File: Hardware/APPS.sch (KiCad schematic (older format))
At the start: 20 parts, among them SW1 SW_Push, U1 STM32F103C8Tx, Y1 Crystal 8 MHz

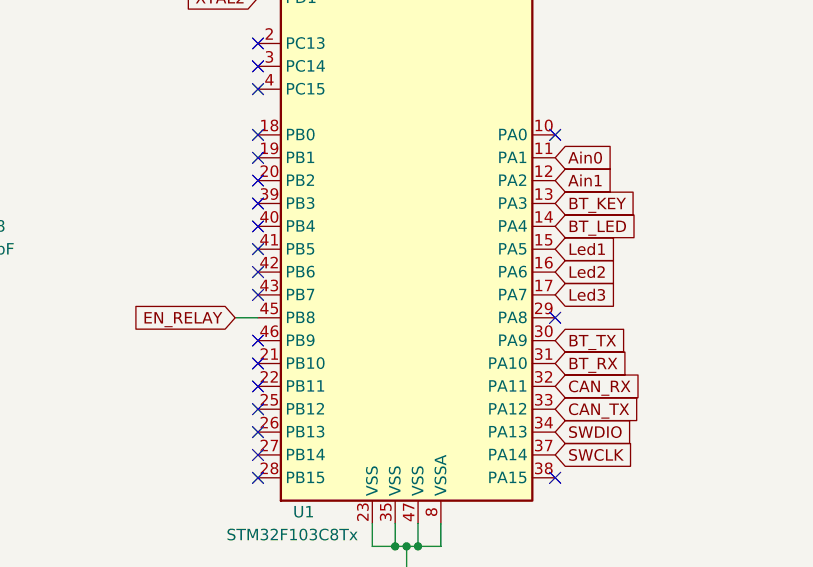
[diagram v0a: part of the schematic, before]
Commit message: Positioned Bluetooth module
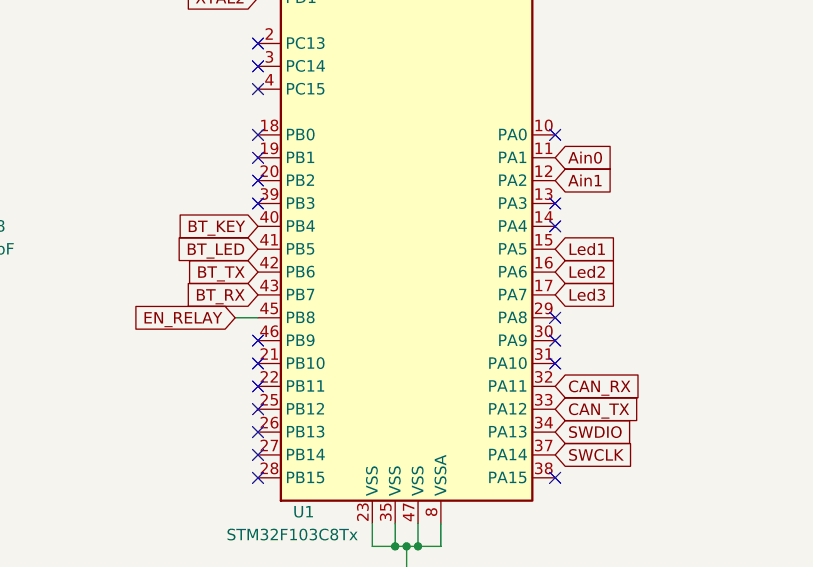
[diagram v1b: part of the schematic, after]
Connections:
- net BT_KEY: now also U1.40 (PB4); no longer U1.13 (PA3)
- net BT_LED: now also U1.41 (PB5); no longer U1.14 (PA4)
- net BT_RX: now also U1.43 (PB7); no longer U1.31 (PA10)
- net BT_TX: now also U1.42 (PB6); no longer U1.30 (PA9)
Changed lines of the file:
@@
 EESchema Schematic File Version 4
-LIBS:APPS-cache
-EELAYER 29 0
+EELAYER 30 0
 EELAYER END
 $Descr A4 11693 8268
@@
 Text GLabel 5500 5050 2    50   Input ~ 0
 SWCLK
-Text GLabel 5500 4750 2    50   Input ~ 0
-CAN_RX
 Wire Wire Line
 	3250 2550 3250 2300
@@
 NoConn ~ 4200 4650
 NoConn ~ 4200 4550
-NoConn ~ 4200 4350
-NoConn ~ 4200 4250
-NoConn ~ 4200 4150
-NoConn ~ 4200 4050
+NoConn ~ 5500 4050
+NoConn ~ 5500 3950
 NoConn ~ 4200 3950
 NoConn ~ 4200 3850
@@
 Text Notes 7850 2700 0    50   ~ 0
 Debugging Diodes
-Text GLabel 5500 4650 2    50   Input ~ 0
+Text GLabel 4200 4350 0    50   Input ~ 0
 BT_RX
-Text GLabel 5500 4550 2    50   Input ~ 0
+Text GLabel 4200 4250 0    50   Input ~ 0
 BT_TX
 Text GLabel 5500 4150 2    50   Input ~ 0
 Led1
-Text GLabel 5500 3950 2    50   Input ~ 0
+Text GLabel 4200 4050 0    50   Input ~ 0
 BT_KEY
-Text GLabel 5500 4050 2    50   Input ~ 0
+Text GLabel 4200 4150 0    50   Input ~ 0
 BT_LED
+NoConn ~ 5500 4550
+NoConn ~ 5500 4650
+Text GLabel 5500 4750 2    50   Input ~ 0
+CAN_RX
 $EndSCHEMATC

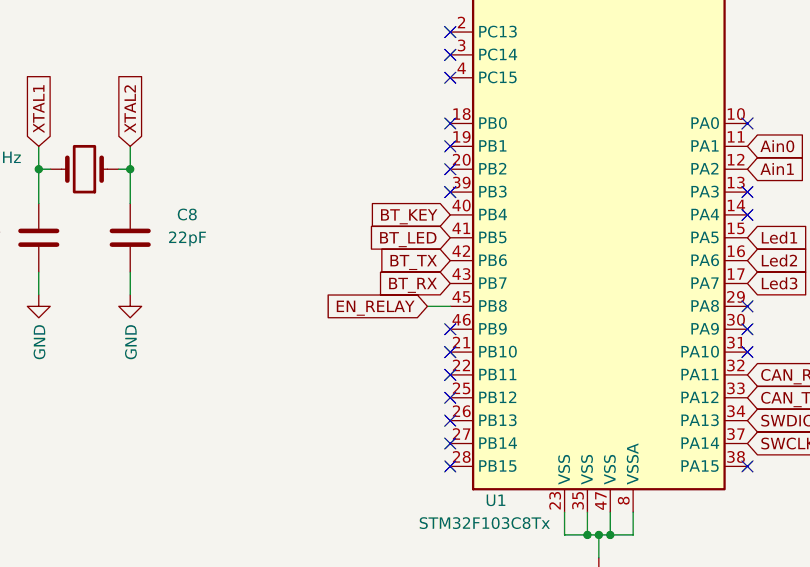
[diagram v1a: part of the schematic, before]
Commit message: Changed HC-05 pins for other Forbot HC-05
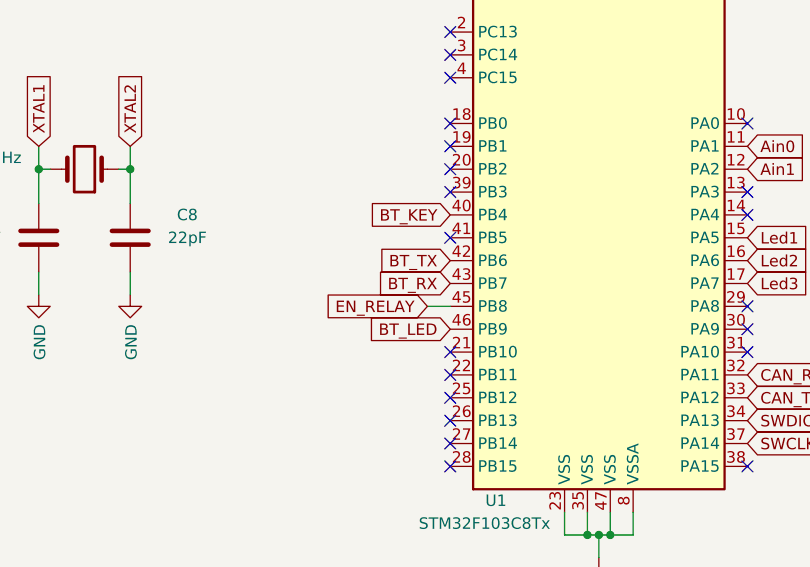
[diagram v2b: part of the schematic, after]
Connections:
- net BT_LED: now also U1.46 (PB9); no longer U1.41 (PB5)
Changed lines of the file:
@@
 NoConn ~ 4200 4750
 NoConn ~ 4200 4650
-NoConn ~ 4200 4550
+NoConn ~ 4200 4150
 NoConn ~ 5500 4050
 NoConn ~ 5500 3950
@@
 Text GLabel 4200 4050 0    50   Input ~ 0
 BT_KEY
-Text GLabel 4200 4150 0    50   Input ~ 0
+Text GLabel 4200 4550 0    50   Input ~ 0
 BT_LED
 NoConn ~ 5500 4550

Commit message: Quick fixes
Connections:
- net BT_KEY: now also U1.46 (PB9); no longer U1.40 (PB4)
- net BT_LED: now also U1.40 (PB4); no longer U1.46 (PB9)
- net BT_RX: now also U1.42 (PB6); no longer U1.43 (PB7)
- net BT_TX: now also U1.43 (PB7); no longer U1.42 (PB6)
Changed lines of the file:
@@
 NoConn ~ 4200 4850
 NoConn ~ 4200 4750
-NoConn ~ 4200 4650
-NoConn ~ 4200 4150
 NoConn ~ 5500 4050
 NoConn ~ 5500 3950
@@
 Text Notes 7850 2700 0    50   ~ 0
 Debugging Diodes
-Text GLabel 4200 4350 0    50   Input ~ 0
-BT_RX
-Text GLabel 4200 4250 0    50   Input ~ 0
-BT_TX
 Text GLabel 5500 4150 2    50   Input ~ 0
 Led1
-Text GLabel 4200 4050 0    50   Input ~ 0
-BT_KEY
-Text GLabel 4200 4550 0    50   Input ~ 0
-BT_LED
 NoConn ~ 5500 4550
 NoConn ~ 5500 4650
 Text GLabel 5500 4750 2    50   Input ~ 0
 CAN_RX
+Text GLabel 4200 4550 0    50   Input ~ 0
+BT_KEY
+NoConn ~ 4200 4650
+Text GLabel 4200 4250 0    50   Input ~ 0
+BT_RX
+Text GLabel 4200 4350 0    50   Input ~ 0
+BT_TX
+NoConn ~ 4200 4150
+Text GLabel 4200 4050 0    50   Input ~ 0
+BT_LED
 $EndSCHEMATC

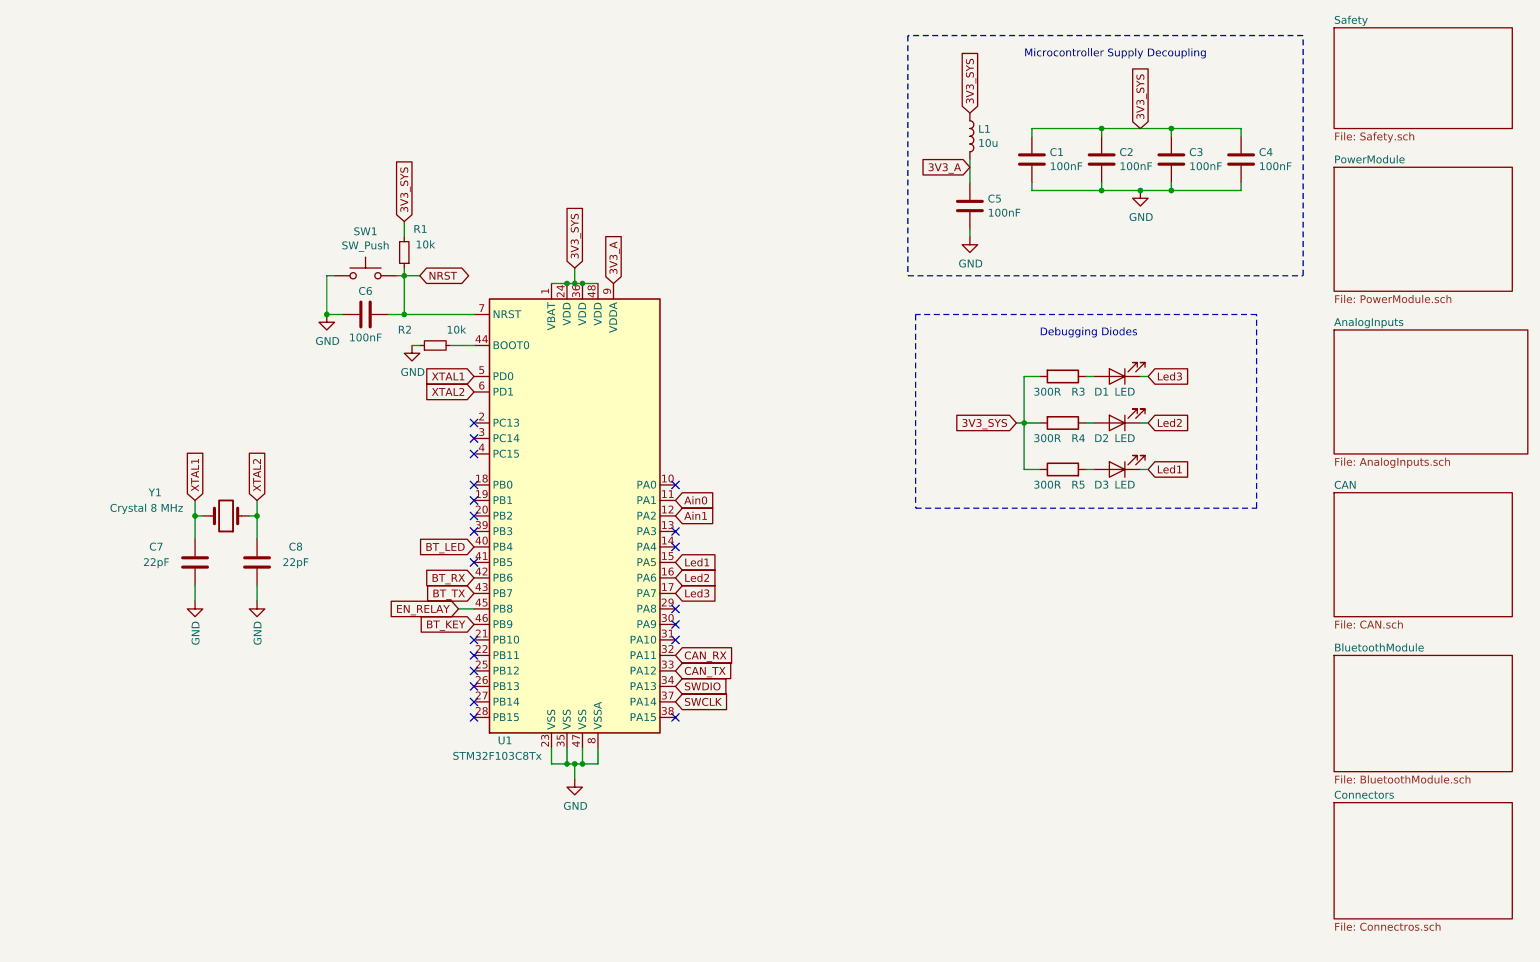
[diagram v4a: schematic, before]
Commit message: Components labels placed
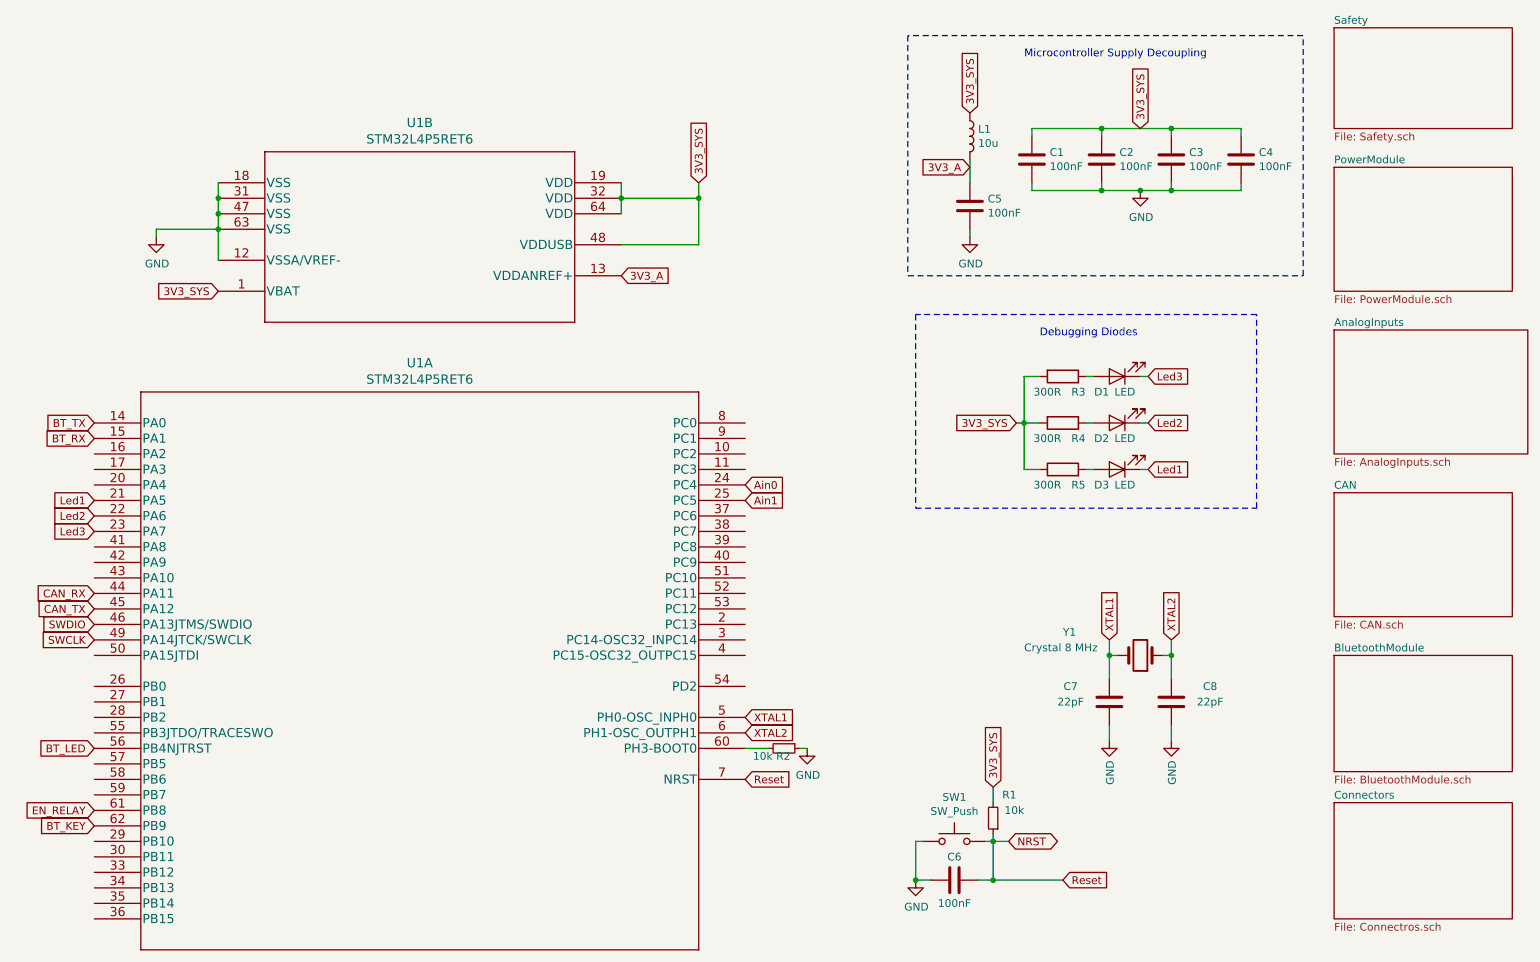
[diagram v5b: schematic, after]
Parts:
- removed U1: STM32F103C8Tx, Package_QFP:LQFP-48_7x7mm_P0.5mm, symbol MCU_ST_STM32F1:STM32F103C8Tx
- added U1: STM32L4P5RET6, footprints:STM32L4P5RET6, symbol 2021-05-10_08-39-16:STM32L4P5RET6
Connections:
- net 3V3_A: now also U1.13 (VDDANREF+)
- net 3V3_SYS: now also U1.1 (VBAT), U1.19 (VDD), U1.32 (VDD), U1.48 (VDDUSB), U1.64 (VDD)
- net Ain0: now also U1.24 (PC4)
- net Ain1: now also U1.25 (PC5)
- net BT_KEY: now also U1.62 (PB9)
- net BT_LED: now also U1.56 (PB4NJTRST)
- net BT_RX: now also U1.15 (PA1)
- net BT_TX: now also U1.14 (PA0)
- net CAN_RX: now also U1.44 (PA11)
- net CAN_TX: now also U1.45 (PA12)
- net EN_RELAY: now also U1.61 (PB8)
- net GND: now also U1.12 (VSSA/VREF-), U1.18 (VSS), U1.31 (VSS), U1.47 (VSS), U1.63 (VSS)
- net Led1: now also U1.21 (PA5)
- net Led2: now also U1.22 (PA6)
- net Led3: now also U1.23 (PA7)
- net NRST: now also U1.7 (NRST)
- net SWCLK: now also U1.49 (PA14JTCK/SWCLK)
- net SWDIO: now also U1.46 (PA13JTMS/SWDIO)
- net XTAL1: now also U1.5 (PH0-OSC_INPH0)
- net XTAL2: now also U1.6 (PH1-OSC_OUTPH1)
- net at R2.2: now also U1.60 (PH3-BOOT0)
- no-connect marks 21 -> 0
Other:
- moved on the sheet: C6, C7, C8, R1, R2, SW1, Y1
